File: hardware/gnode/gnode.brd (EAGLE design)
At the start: 50 x 25 mm, 22 parts, among them IC1 HTU21D, U1 ATMEGA328P_TQFP

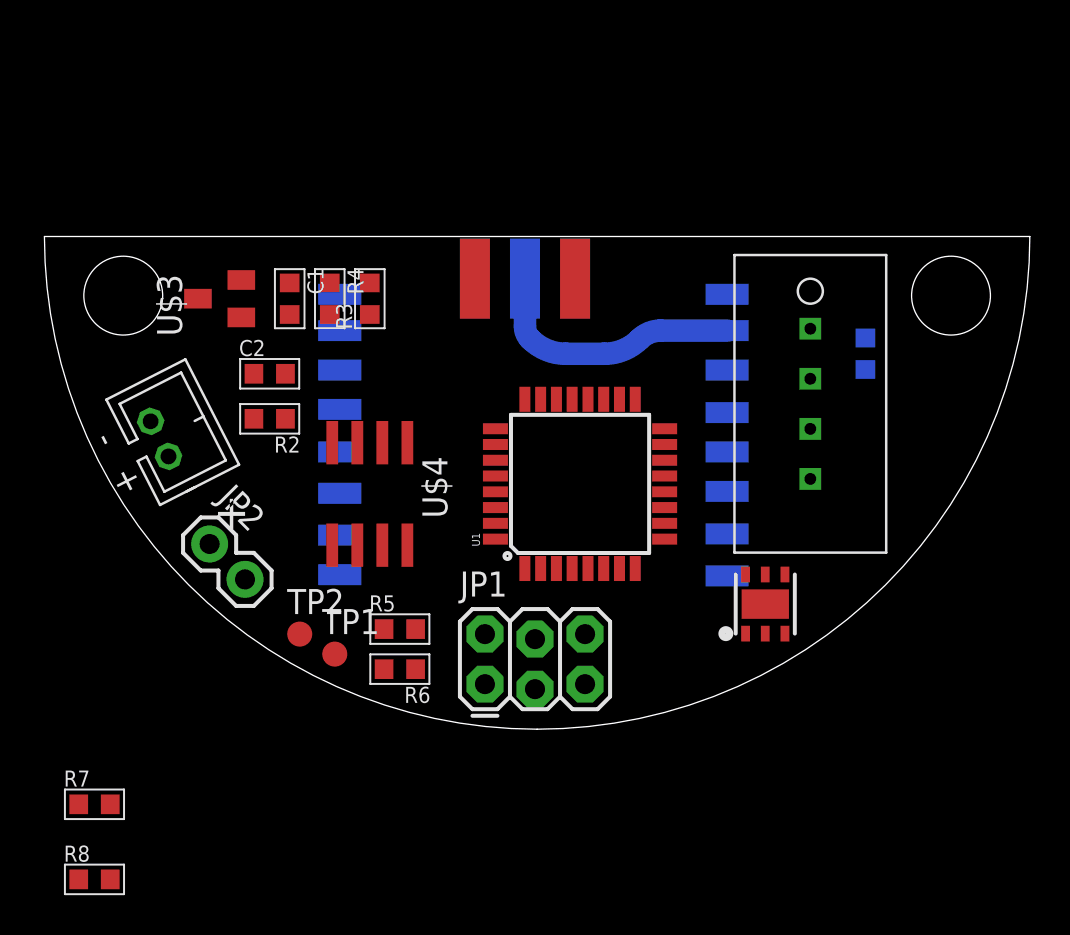
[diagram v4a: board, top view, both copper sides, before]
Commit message: centred the sma connector, placed resistors for sense potdivs
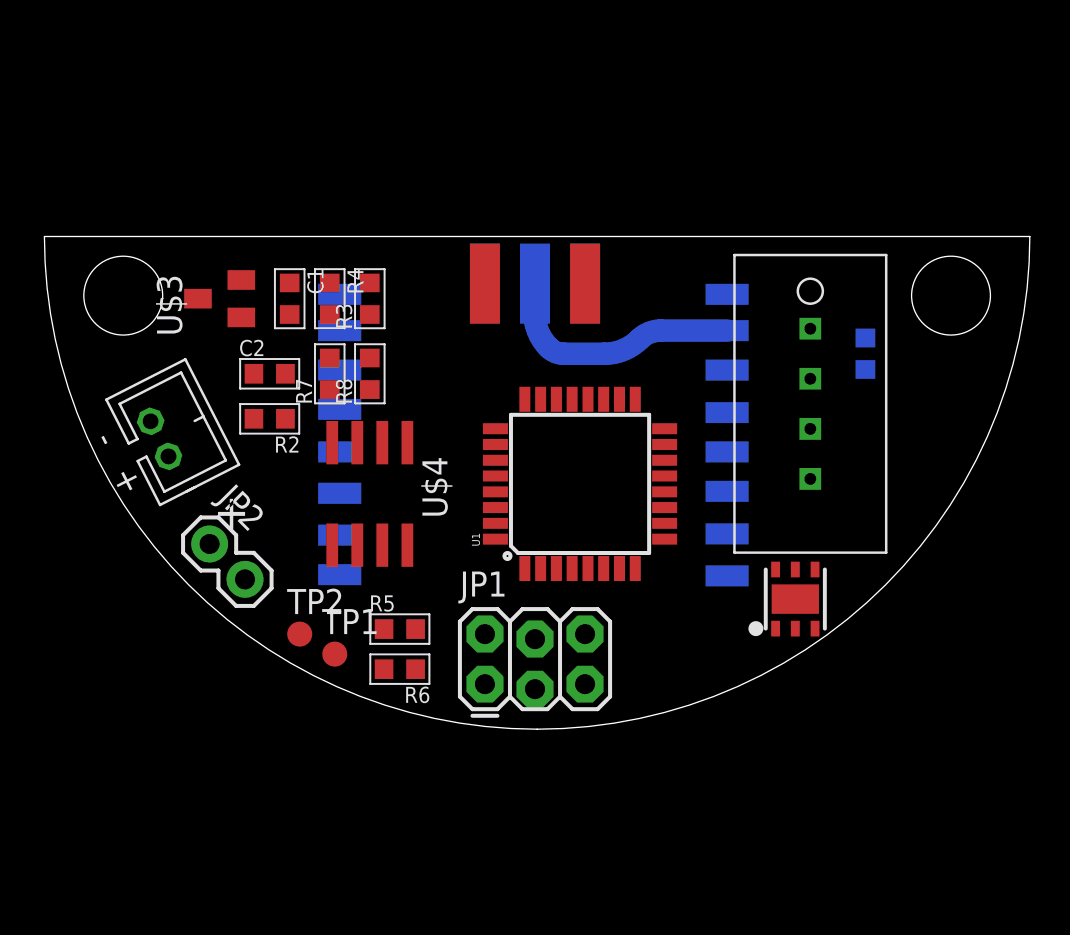
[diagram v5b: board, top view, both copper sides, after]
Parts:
- moved R8 29.2 mm to (16.5, 18.0), turned to 90 degrees
- moved R7 24.9 mm to (14.5, 18.0), turned to 90 degrees
- moved IC1 1.55 mm to (38.1, 6.60)
- moved J$1 0.57 mm to (27.4, 22.6)
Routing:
- net N$1: track 13.5 -> 12.7 mm

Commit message: routed
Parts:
- removed U$2: DHT22_PTH, jonsowman:DHT22
- added C3: 100n, passives-7351:C0603-N
- added JP3: (no value), SparkFun-Connectors:1X04
- added U2: (no value), RHT03_DHT-22_AM2302:RHT03_DHT-22
- moved IC1 6.04 mm to (32.5, 4.32), turned to 270 degrees
- moved R1 5.14 mm to (39.9, 14.2), turned to 270 degrees
- moved J1 1.44 mm to (6.86, 15.7), turned to 117 degrees
- moved U1 1.30 mm to (25.9, 12.2)
- moved JP2 1.27 mm to (9.40, 10.2)
- moved TP1 1.05 mm to (15.0, 4.83)
- turned C1 to 90 degrees
- turned C2 to 180 degrees
- turned R2 to 0 degrees
- turned R8 to 270 degrees
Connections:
- new net GPIO0: JP3.3, U1.10
- new net GPIO1: JP3.4, U1.11
- net DHT22_DATA: now also U2.DATA; no longer U$2.DATA
- net DHT22_VCC: now also U2.VDD; no longer U$2.VCC
- net GND: now also C3.2, JP3.2, U2.GND; no longer U$2.GND
- net VCC: now also C3.1, IC1.5, JP3.1
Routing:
- net VCC: track 0.00 -> 112.3 mm
- net VBATT: track 0.00 -> 43.6 mm
- net SCK: track 0.00 -> 40.8 mm, vias 0 -> 1
- net SHT_SCK: track 0.00 -> 37.3 mm, vias 0 -> 2
- net MISO: track 0.00 -> 31.2 mm, vias 0 -> 1
- net NRST: track 0.00 -> 26.0 mm
- net MOSI: track 0.00 -> 24.6 mm, vias 0 -> 1
- net VPANEL: track 0.00 -> 16.3 mm
- net DHT22_VCC: track 0.00 -> 14.6 mm
- net RFM_DIO0: track 0.00 -> 14.4 mm, vias 0 -> 1
- net DHT22_DATA: track 0.00 -> 14.1 mm
- net SHT_DATA: track 0.00 -> 13.9 mm, vias 0 -> 2
- net N$5: track 0.00 -> 12.9 mm
- net VSENSE_BATT: track 0.00 -> 11.8 mm
- net GND: track 0.00 -> 9.18 mm, vias 0 -> 31
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- added copper zone on layer 1, net GND
- added copper zone on layer 16, net GND
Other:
- board text added: "+PV"
- board text added: "APR 15"
- board text added: "BAT"
- board text added: "DHT22"
- board text added: "ICSP"
- board text added: "J. COXON"
- board text added: "J. SOWMAN"
- board text added: "TP"
- board text added: "ukhas.net"
- board text removed: "+"

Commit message: tidying
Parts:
- added C4: 100n, passives-7351:C0603-N
- moved JP3 3.30 mm to (45.7, 17.3), turned to 240 degrees
- moved TP2 0.57 mm to (13.2, 5.33)
- moved TP1 0.51 mm to (15.0, 5.33)
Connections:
- net GND: now also C4.2
- net VCC: now also C4.1
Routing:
- net VCC: track 112.3 -> 116.5 mm
- net N$5: track 12.9 -> 11.8 mm

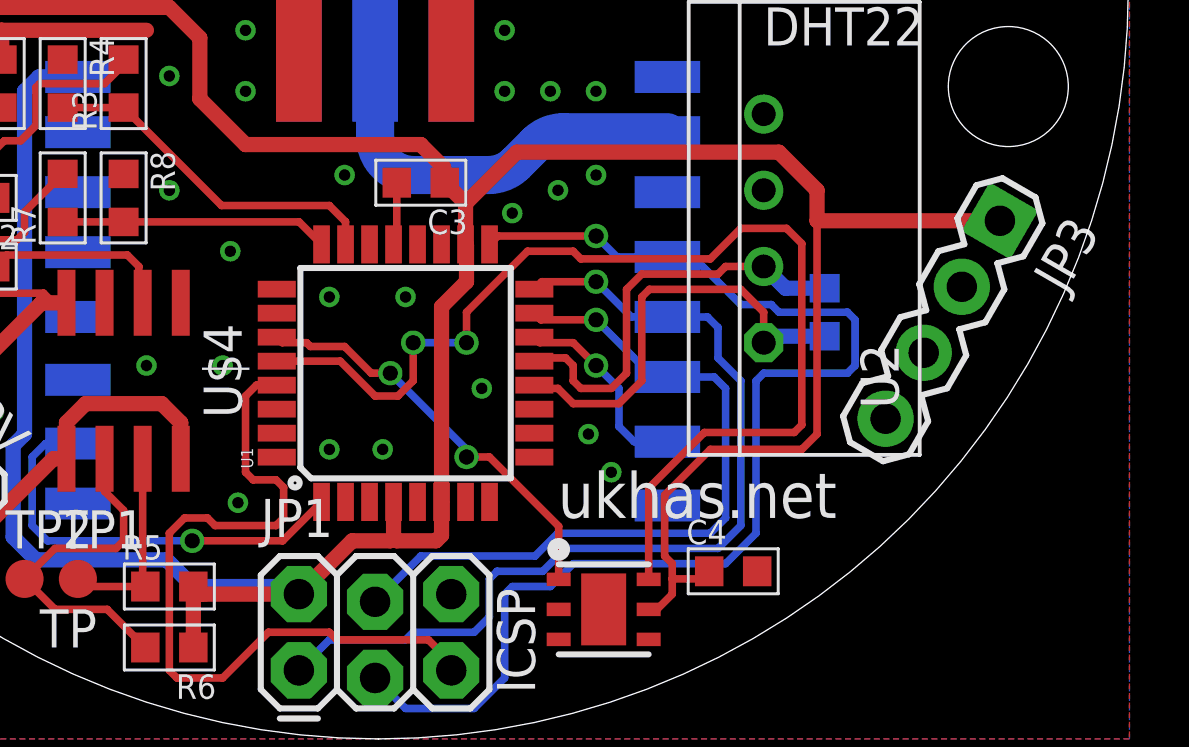
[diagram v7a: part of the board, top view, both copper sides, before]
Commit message: routed gpio for adc/pwm
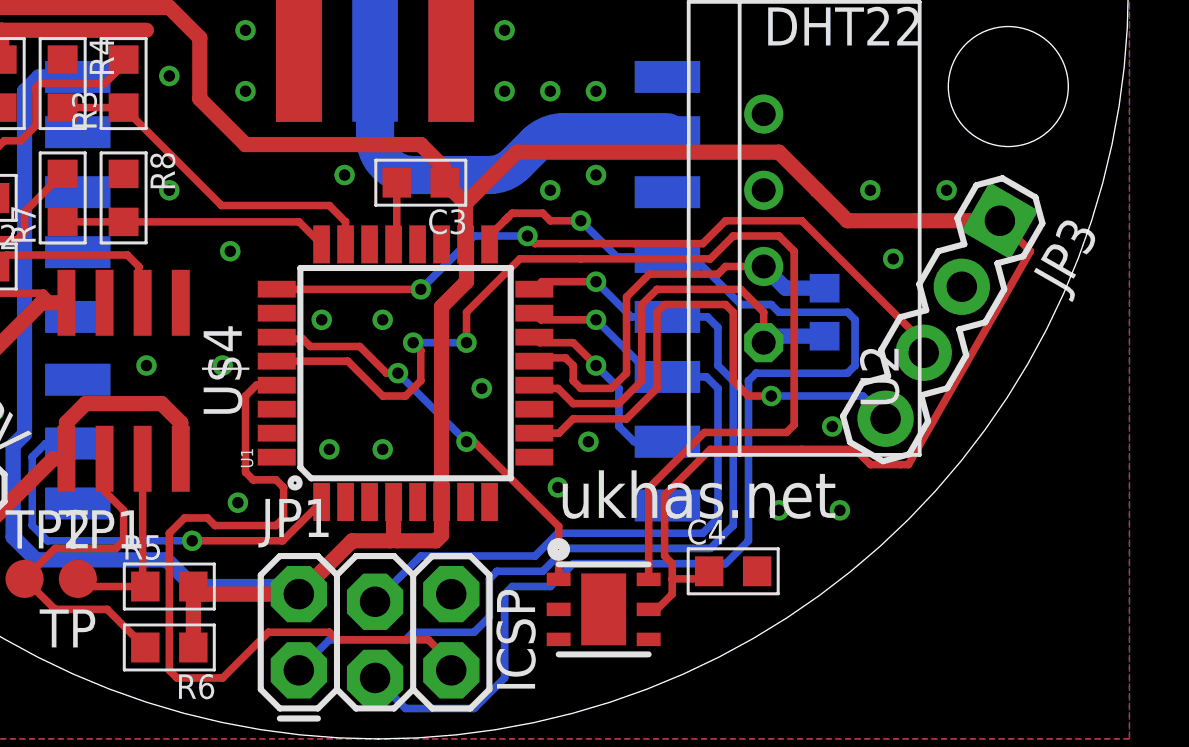
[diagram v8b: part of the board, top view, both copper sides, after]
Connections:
- net GPIO0: now also JP3.4; no longer JP3.3
- net GPIO1: now also JP3.3, U1.25; no longer JP3.4, U1.11
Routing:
- net GPIO1: track 0.00 -> 24.7 mm, vias 0 -> 2
- net GPIO0: track 0.00 -> 17.9 mm, vias 0 -> 1
- net VCC: track 116.5 -> 121.4 mm
- net SCK: track 40.8 -> 41.9 mm
- net SHT_SCK: track 37.1 -> 36.4 mm
- net MOSI: track 24.6 -> 24.1 mm
- net GND: vias 31 -> 36
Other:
- board text added: "GND"
- board text added: "PC2"
- board text added: "PD6"
- board text added: "VCC"
